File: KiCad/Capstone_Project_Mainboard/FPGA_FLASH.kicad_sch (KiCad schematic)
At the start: 8 parts

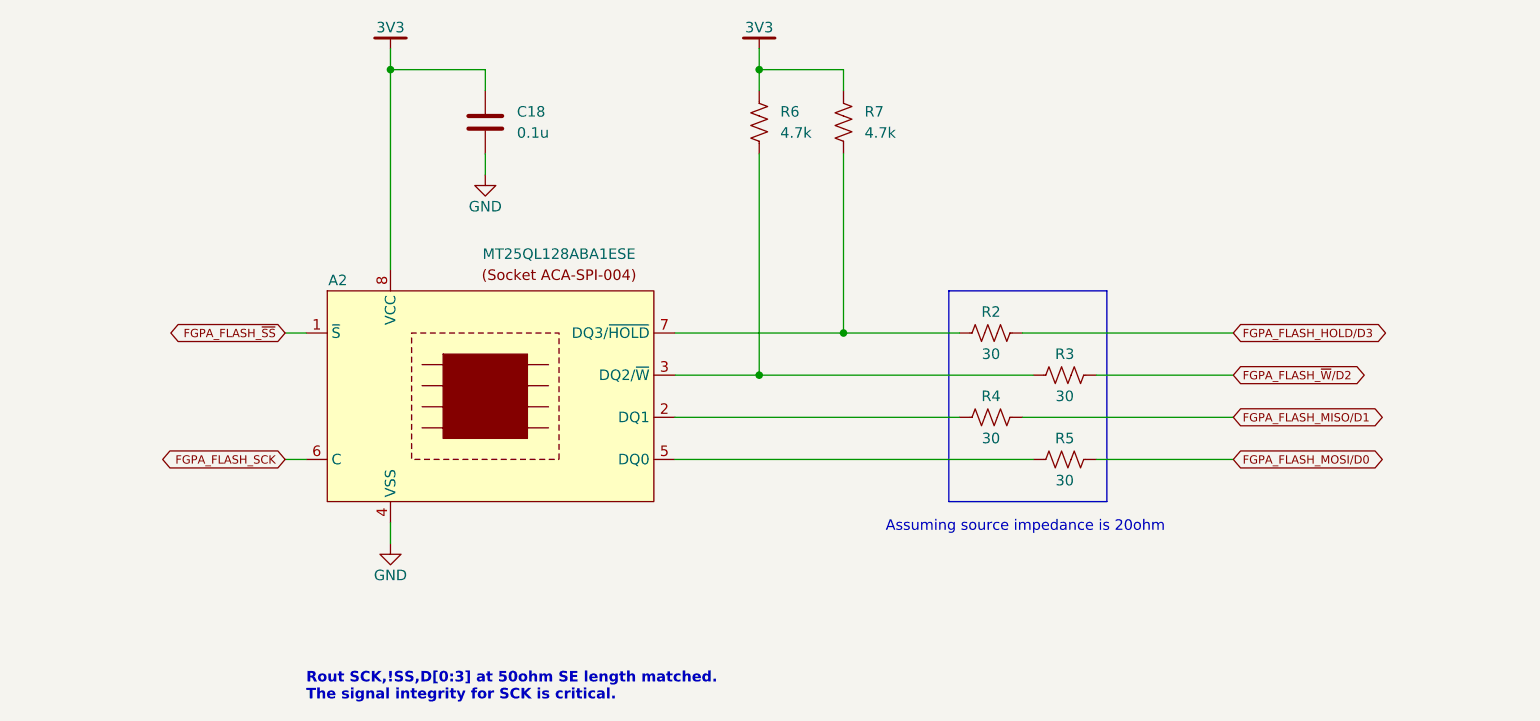
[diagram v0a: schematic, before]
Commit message: Updated FPGA Footprint
Added die-to-pad length offsets to all pins of the FFG676 package. These values were derived from the delay files provided in Vivado.
+ Other minor bugfixes
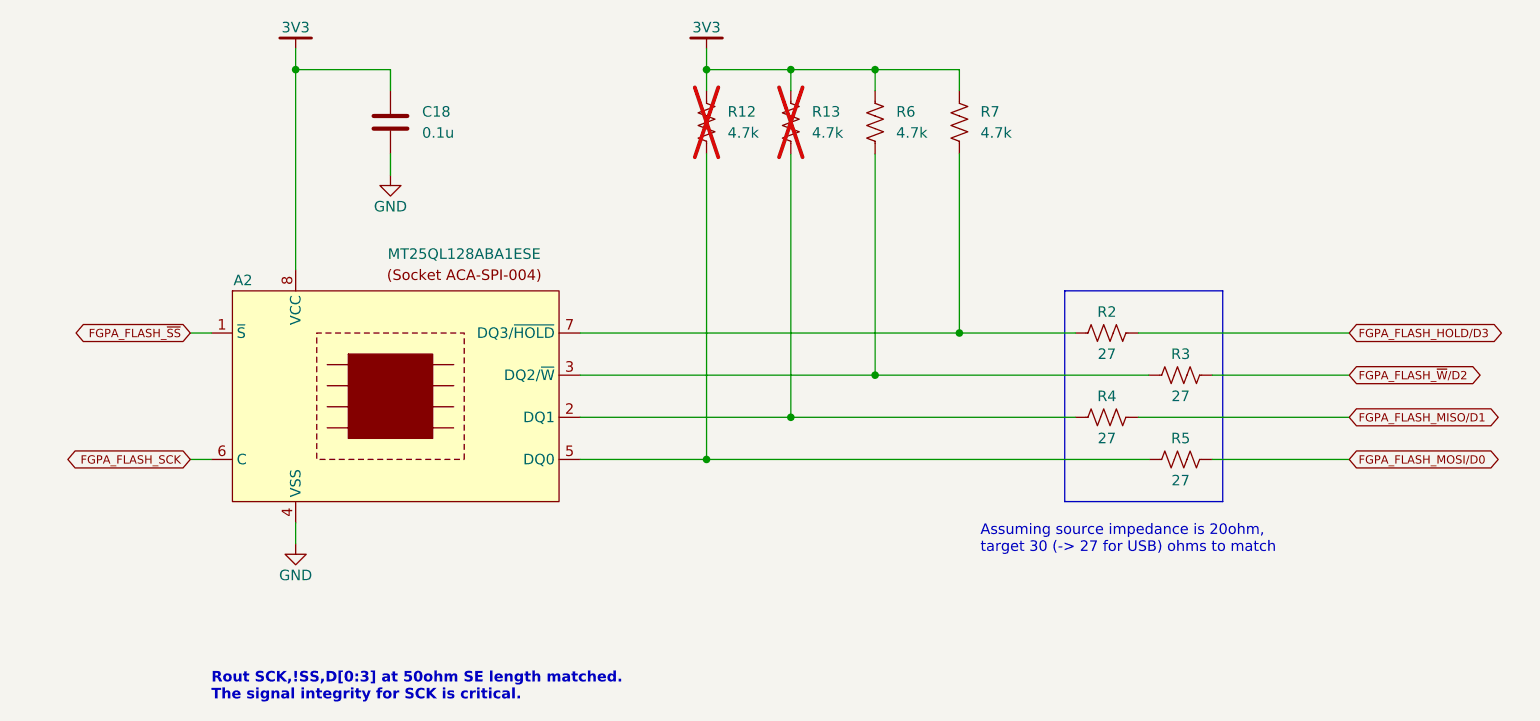
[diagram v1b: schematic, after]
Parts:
- added R12, R13: 4.7k, symbol Device:R_US
- R2, R3, R4, R5: value 30 -> 27
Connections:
- net 3V3: now also R12.1, R13.1
- net at A2.2 (DQ1), R4.1: now also R13.2
- net at A2.5 (DQ0), R5.1: now also R12.2
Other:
- note added: "Assuming source impedance is 20ohm, target 30 (-> 27 for USB) ohms to match"
- note removed: "Assuming source impedance is 20ohm"
- moved on the sheet: A2, C18, R2, R3, R4, R5, R6, R7

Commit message: Core non-power parts defined
Most major non-power components added to KiCad project
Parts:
- added R9: 4.7k, Resistor_SMD:R_0402_1005Metric, symbol Device:R_US
- C18: footprint (none) -> Capacitor_SMD:C_0402_1005Metric; Part Number (none) -> GRM155R71E104ME14J
- R12, R13, R6, R7: footprint (none) -> Resistor_SMD:R_0402_1005Metric; Part Number (none) -> RC0402FR-074K7L
- R2, R3, R4, R5: footprint (none) -> Resistor_SMD:R_0402_1005Metric; Part Number (none) -> RC0402FR-7W27RL
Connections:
- net 3V3: now also R9.1
- net FGPA_FLASH_HOLD/D3 renamed FPGA_FLASH_HOLD/D3
- net FGPA_FLASH_MISO/D1 renamed FPGA_FLASH_MISO/D1
- net FGPA_FLASH_MOSI/D0 renamed FPGA_FLASH_MOSI/D0
- net FGPA_FLASH_SCK renamed FPGA_FLASH_SCK
- net FGPA_FLASH_~{SS} renamed FPGA_FLASH_~{SS}
- net FPGA_FLASH_~{SS}: now also R9.2
- net FGPA_FLASH_~{W}/D2 renamed FPGA_FLASH_~{W}/D2
